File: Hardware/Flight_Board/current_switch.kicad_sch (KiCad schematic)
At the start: 21 parts, among them U8 TPS274160A

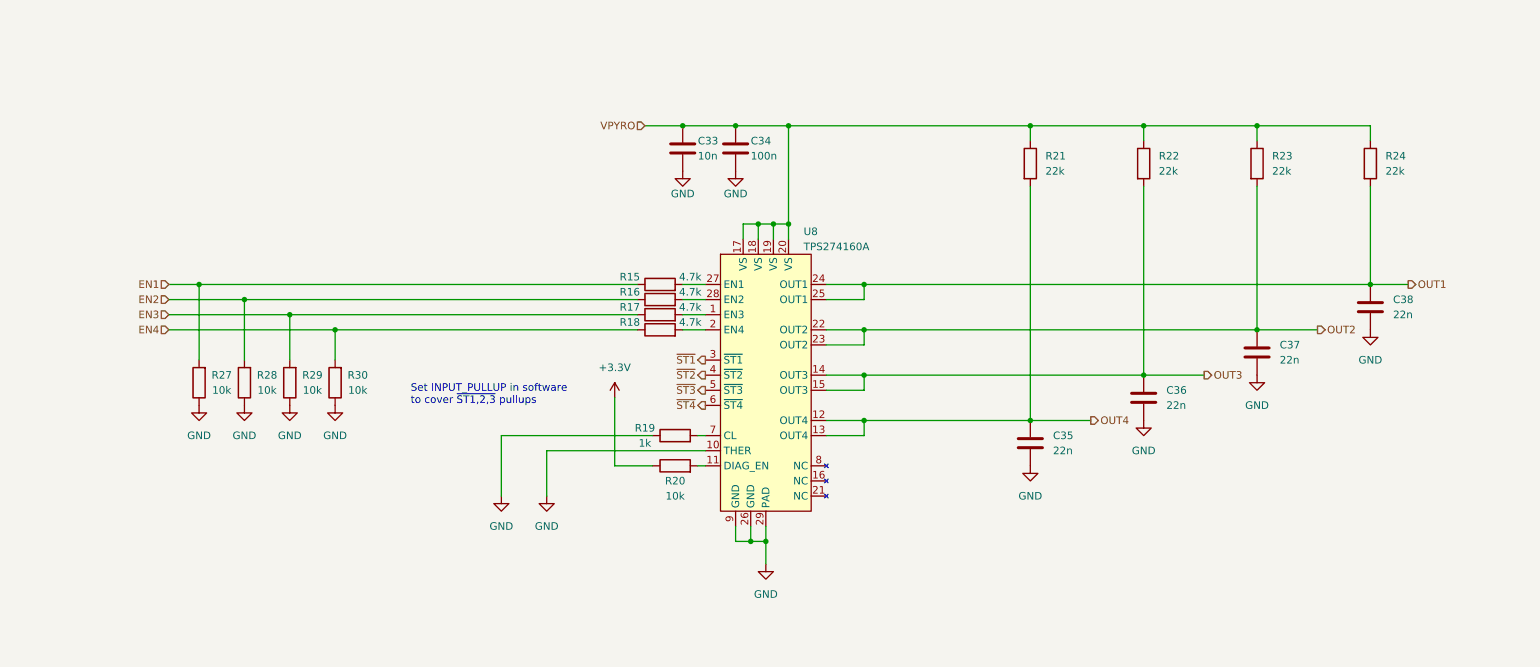
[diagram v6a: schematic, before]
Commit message: Add LEDs and test points
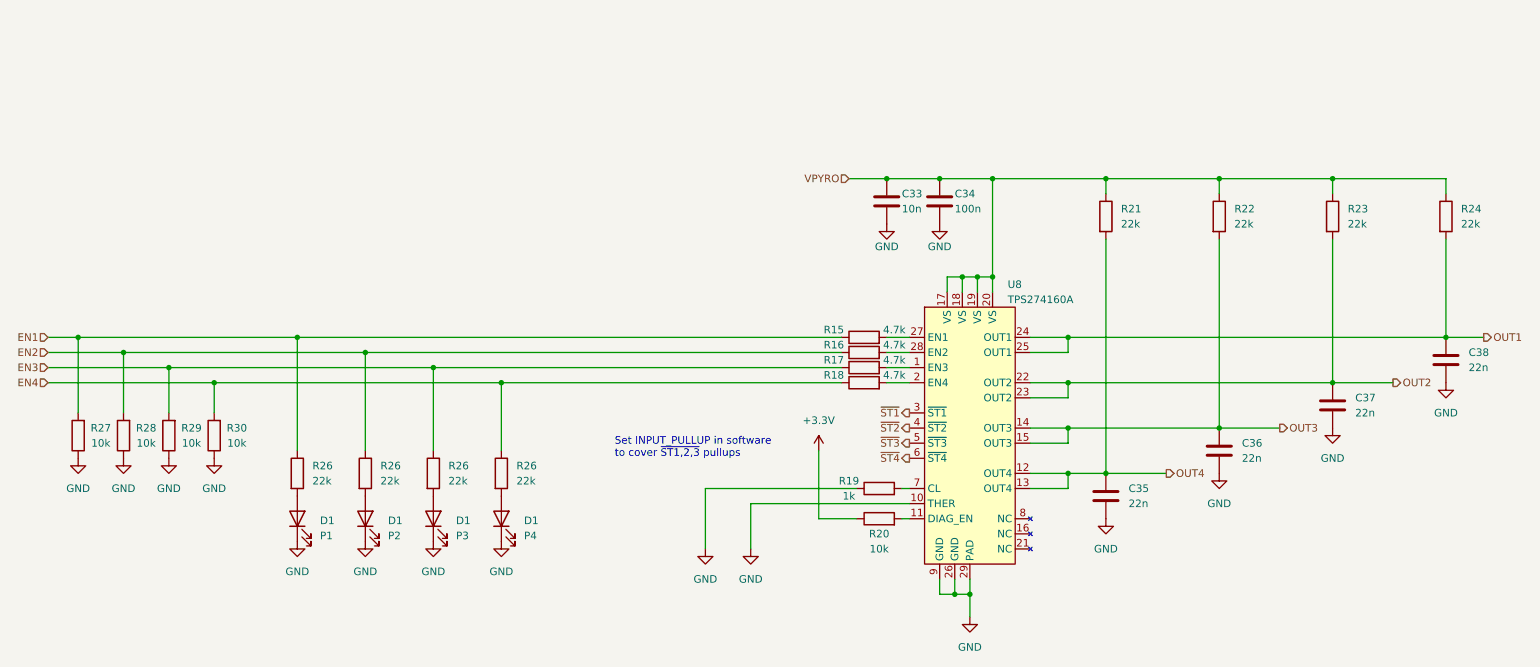
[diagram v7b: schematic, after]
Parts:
- added D1: P1, symbol Device:LED
- added D1: P4, symbol Device:LED
- added D1: P2, symbol Device:LED
- added D1: P3, symbol Device:LED
- added R26 (x4): 22k, symbol Device:R
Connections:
- net EN1: now also R26.1
- net EN2: now also R26.1
- net EN3: now also R26.1
- net EN4: now also R26.1
- net GND: now also D1.1 (K), D1.1 (K), D1.1 (K), D1.1 (K)
- new net: D1.2 (A), R26.2 (x4)
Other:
- moved on the sheet: C33, C34, C35, C36, C37, C38, R15, R16, R17, R18, R19, R20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

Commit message: final touches, bom, footprints
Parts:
- C33, C34, C35, C36, C37, C38: footprint (none) -> Capacitor_SMD:C_0603_1608Metric_Pad1.08x0.95mm_HandSolder
- D1: footprint (none) -> LED_SMD:LED_0603_1608Metric_Pad1.05x0.95mm_HandSolder
- R15, R16, R17, R18, R19, R20, R21, R22, R23, R24, R26, R27, R28, R29, R30: footprint (none) -> Resistor_SMD:R_0603_1608Metric_Pad0.98x0.95mm_HandSolder
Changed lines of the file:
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@@
       (effects (font (size 1.27 1.27)) (justify left))
     )
-    (property "Footprint" "" (at 206.7052 114.3 0)
+    (property "Footprint" "Capacitor_SMD:C_0603_1608Metric_Pad1.08x0.95mm_HandSolder" (at 206.7052 114.3 0)
       (effects (font (size 1.27 1.27)) hide)
     )
@@
       (effects (font (size 1.27 1.27)) (justify right))
     )
-    (property "Footprint" "" (at 69.85 114.3 0)
+    (property "Footprint" "LED_SMD:LED_0603_1608Metric_Pad1.05x0.95mm_HandSolder" (at 69.85 114.3 0)
       (effects (font (size 1.27 1.27)) hide)
     )
@@
       (effects (font (size 1.27 1.27)) (justify left))
     )
-    (property "Footprint" "" (at 242.062 63.5 90)
+    (property "Footprint" "Resistor_SMD:R_0603_1608Metric_Pad0.98x0.95mm_HandSolder" (at 242.062 63.5 90)
       (effects (font (size 1.27 1.27)) hide)
     )
@@
       (effects (font (size 1.27 1.27)) (justify left))
     )
-    (property "Footprint" "" (at 203.962 63.5 90)
+    (property "Footprint" "Resistor_SMD:R_0603_1608Metric_Pad0.98x0.95mm_HandSolder" (at 203.962 63.5 90)
       (effects (font (size 1.27 1.27)) hide)
     )
@@
       (effects (font (size 1.27 1.27)))
     )
-    (property "Footprint" "" (at 34.798 100.33 90)
+    (property "Footprint" "Resistor_SMD:R_0603_1608Metric_Pad0.98x0.95mm_HandSolder" (at 34.798 100.33 90)
       (effects (font (size 1.27 1.27)) hide)
     )
@@
       (effects (font (size 1.27 1.27)) (justify left))
     )
-    (property "Footprint" "" (at 223.012 63.5 90)
+    (property "Footprint" "Resistor_SMD:R_0603_1608Metric_Pad0.98x0.95mm_HandSolder" (at 223.012 63.5 90)
       (effects (font (size 1.27 1.27)) hide)
     )
@@
       (effects (font (size 1.27 1.27)) (justify left))
     )
-    (property "Footprint" "" (at 244.8052 99.06 0)
+    (property "Footprint" "Capacitor_SMD:C_0603_1608Metric_Pad1.08x0.95mm_HandSolder" (at 244.8052 99.06 0)
       (effects (font (size 1.27 1.27)) hide)
     )
@@
       (effects (font (size 1.27 1.27)) (justify left))
     )
-    (property "Footprint" "" (at 79.502 106.68 90)
+    (property "Footprint" "Resistor_SMD:R_0603_1608Metric_Pad0.98x0.95mm_HandSolder" (at 79.502 106.68 90)
       (effects (font (size 1.27 1.27)) hide)
     )
@@
       (effects (font (size 1.27 1.27)) (justify left))
     )
-    (property "Footprint" "" (at 102.362 106.68 90)
+    (property "Footprint" "Resistor_SMD:R_0603_1608Metric_Pad0.98x0.95mm_HandSolder" (at 102.362 106.68 90)
       (effects (font (size 1.27 1.27)) hide)
     )
@@
       (effects (font (size 1.27 1.27)) (justify left))
     )
-    (property "Footprint" "" (at 90.932 106.68 90)
+    (property "Footprint" "Resistor_SMD:R_0603_1608Metric_Pad0.98x0.95mm_HandSolder" (at 90.932 106.68 90)
       (effects (font (size 1.27 1.27)) hide)
     )
@@
       (effects (font (size 1.27 1.27)) (justify left))
     )
-    (property "Footprint" "" (at 178.7652 64.77 0)
+    (property "Footprint" "Capacitor_SMD:C_0603_1608Metric_Pad1.08x0.95mm_HandSolder" (at 178.7652 64.77 0)
       (effects (font (size 1.27 1.27)) hide)
     )
@@
       (effects (font (size 1.27 1.27)) (justify right))
     )
-    (property "Footprint" "" (at 104.14 114.3 0)
+    (property "Footprint" "LED_SMD:LED_0603_1608Metric_Pad1.05x0.95mm_HandSolder" (at 104.14 114.3 0)
       (effects (font (size 1.27 1.27)) hide)
     )
@@
       (effects (font (size 1.27 1.27)) (justify left))
     )
-    (property "Footprint" "" (at 263.8552 91.44 0)
+    (property "Footprint" "Capacitor_SMD:C_0603_1608Metric_Pad1.08x0.95mm_HandSolder" (at 263.8552 91.44 0)
       (effects (font (size 1.27 1.27)) hide)
     )
@@
       (effects (font (size 1.27 1.27)) (justify left))
     )
-    (property "Footprint" "" (at 68.072 106.68 90)
+    (property "Footprint" "Resistor_SMD:R_0603_1608Metric_Pad0.98x0.95mm_HandSolder" (at 68.072 106.68 90)
       (effects (font (size 1.27 1.27)) hide)
     )
@@
       (effects (font (size 1.27 1.27)))
     )
-    (property "Footprint" "" (at 167.64 116.078 90)
+    (property "Footprint" "Resistor_SMD:R_0603_1608Metric_Pad0.98x0.95mm_HandSolder" (at 167.64 116.078 90)
       (effects (font (size 1.27 1.27)) hide)
     )
@@
       (effects (font (size 1.27 1.27)) (justify left))
     )
-    (property "Footprint" "" (at 169.8752 64.77 0)
+    (property "Footprint" "Capacitor_SMD:C_0603_1608Metric_Pad1.08x0.95mm_HandSolder" (at 169.8752 64.77 0)
       (effects (font (size 1.27 1.27)) hide)
     )
@@
       (effects (font (size 1.27 1.27)))
     )
-    (property "Footprint" "" (at 165.1 93.218 90)
+    (property "Footprint" "Resistor_SMD:R_0603_1608Metric_Pad0.98x0.95mm_HandSolder" (at 165.1 93.218 90)
       (effects (font (size 1.27 1.27)) hide)
     )
@@
       (effects (font (size 1.27 1.27)))
     )
-    (property "Footprint" "" (at 165.1 88.138 90)
+    (property "Footprint" "Resistor_SMD:R_0603_1608Metric_Pad0.98x0.95mm_HandSolder" (at 165.1 88.138 90)
       (effects (font (size 1.27 1.27)) hide)
     )
@@
       (effects (font (size 1.27 1.27)))
     )
-    (property "Footprint" "" (at 167.64 110.998 90)
+    (property "Footprint" "Resistor_SMD:R_0603_1608Metric_Pad0.98x0.95mm_HandSolder" (at 167.64 110.998 90)
       (effects (font (size 1.27 1.27)) hide)
     )
@@
       (effects (font (size 1.27 1.27)) (justify left))
     )
-    (property "Footprint" "" (at 261.112 63.5 90)
+    (property "Footprint" "Resistor_SMD:R_0603_1608Metric_Pad0.98x0.95mm_HandSolder" (at 261.112 63.5 90)
       (effects (font (size 1.27 1.27)) hide)
     )
@@
       (effects (font (size 1.27 1.27)) (justify left))
     )
-    (property "Footprint" "" (at 225.7552 106.68 0)
+    (property "Footprint" "Capacitor_SMD:C_0603_1608Metric_Pad1.08x0.95mm_HandSolder" (at 225.7552 106.68 0)
       (effects (font (size 1.27 1.27)) hide)
     )
@@
       (effects (font (size 1.27 1.27)) (justify right))
     )
-    (property "Footprint" "" (at 81.28 114.3 0)
+    (property "Footprint" "LED_SMD:LED_0603_1608Metric_Pad1.05x0.95mm_HandSolder" (at 81.28 114.3 0)
       (effects (font (size 1.27 1.27)) hide)
     )
@@
       (effects (font (size 1.27 1.27)))
     )
-    (property "Footprint" "" (at 165.1 85.598 90)
+    (property "Footprint" "Resistor_SMD:R_0603_1608Metric_Pad0.98x0.95mm_HandSolder" (at 165.1 85.598 90)
       (effects (font (size 1.27 1.27)) hide)
     )
@@
       (effects (font (size 1.27 1.27)))
     )
-    (property "Footprint" "" (at 50.038 100.33 90)
+    (property "Footprint" "Resistor_SMD:R_0603_1608Metric_Pad0.98x0.95mm_HandSolder" (at 50.038 100.33 90)
       (effects (font (size 1.27 1.27)) hide)
     )
@@
       (effects (font (size 1.27 1.27)))
     )
-    (property "Footprint" "" (at 57.658 100.33 90)
+    (property "Footprint" "Resistor_SMD:R_0603_1608Metric_Pad0.98x0.95mm_HandSolder" (at 57.658 100.33 90)
       (effects (font (size 1.27 1.27)) hide)
     )
@@
       (effects (font (size 1.27 1.27)))
     )
-    (property "Footprint" "" (at 165.1 90.678 90)
+    (property "Footprint" "Resistor_SMD:R_0603_1608Metric_Pad0.98x0.95mm_HandSolder" (at 165.1 90.678 90)
       (effects (font (size 1.27 1.27)) hide)
     )
@@
       (effects (font (size 1.27 1.27)) (justify right))
     )
-    (property "Footprint" "" (at 92.71 114.3 0)
+    (property "Footprint" "LED_SMD:LED_0603_1608Metric_Pad1.05x0.95mm_HandSolder" (at 92.71 114.3 0)
       (effects (font (size 1.27 1.27)) hide)
     )
@@
       (effects (font (size 1.27 1.27)))
     )
-    (property "Footprint" "" (at 42.418 100.33 90)
-      (effects (font (size 1.27 1.27)) hide)
-    )
+    (property "Footprint" "Resistor_SMD:R_0603_1608Metric_Pad0.98x0.95mm_HandSolder" (at 42.418 100.33 90)
+      (effects (font (size 1.27 1.27)) hide)
+    )
